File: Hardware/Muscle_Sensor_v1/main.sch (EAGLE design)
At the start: 31 parts, among them IC1 TL084D, IC2 TL7660D, K1 61000418221, K2 61000418221, U1 AD8221AR

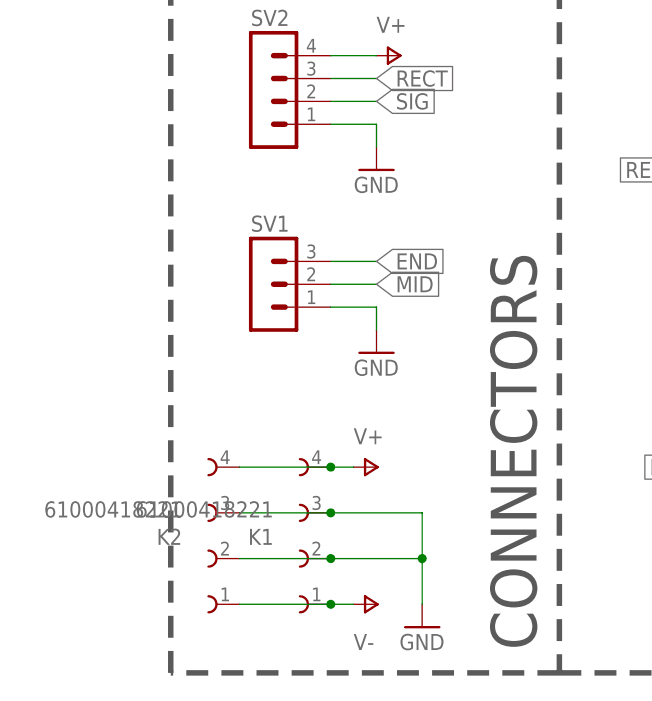
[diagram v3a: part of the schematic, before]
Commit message: Muscle Sensor Updates
Schematic and board updates fixes some bugs of first version.
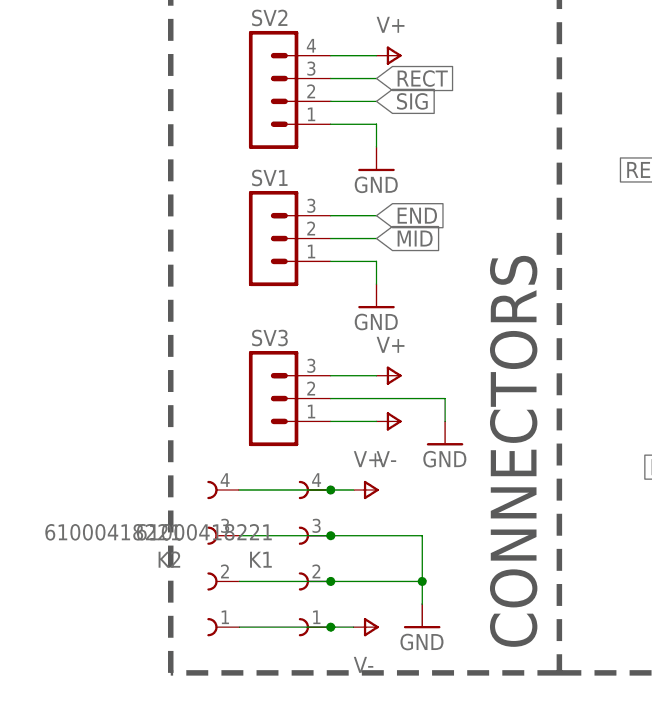
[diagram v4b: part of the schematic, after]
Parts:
- added SV3: (no value), con-lstb:MA03-1
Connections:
- net GND: now also SV3.2
- net V+: now also SV3.3
- net V-: now also SV3.1
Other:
- moved on the sheet: K1, K2, SV1
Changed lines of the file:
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@@
 <part name="H1" library="holes" library_urn="urn:adsk.eagle:library:237" deviceset="MOUNT-HOLE" device="3.0" package3d_urn="urn:adsk.eagle:package:14277/1"/>
 <part name="H2" library="holes" library_urn="urn:adsk.eagle:library:237" deviceset="MOUNT-HOLE" device="3.0" package3d_urn="urn:adsk.eagle:package:14277/1"/>
+<part name="SV3" library="con-lstb" library_urn="urn:adsk.eagle:library:162" deviceset="MA03-1" device="" package3d_urn="urn:adsk.eagle:package:8339/1"/>
+<part name="P+7" library="supply1" library_urn="urn:adsk.eagle:library:371" deviceset="V+" device=""/>
+<part name="GND11" library="supply1" library_urn="urn:adsk.eagle:library:371" deviceset="GND" device=""/>
+<part name="P-5" library="supply1" library_urn="urn:adsk.eagle:library:371" deviceset="V-" device=""/>
 </parts>
 <sheets>
@@
 </instance>
 <instance part="IC1" gate="P" x="5.08" y="114.3" smashed="yes"/>
-<instance part="SV1" gate="G$1" x="5.08" y="45.72" smashed="yes">
-<attribute name="VALUE" x="3.81" y="38.1" size="1.778" layer="96"/>
-<attribute name="NAME" x="3.81" y="51.562" size="1.778" layer="95"/>
-</instance>
-<instance part="P+1" gate="1" x="17.78" y="25.4" smashed="yes" rot="R270">
-<attribute name="VALUE" x="15.24" y="27.94" size="1.778" layer="96"/>
-</instance>
-<instance part="P-1" gate="1" x="17.78" y="10.16" smashed="yes" rot="R90">
-<attribute name="VALUE" x="15.24" y="5.08" size="1.778" layer="96"/>
+<instance part="SV1" gate="G$1" x="5.08" y="50.8" smashed="yes">
+<attribute name="VALUE" x="3.81" y="43.18" size="1.778" layer="96"/>
+<attribute name="NAME" x="3.81" y="56.642" size="1.778" layer="95"/>
+</instance>
+<instance part="P+1" gate="1" x="17.78" y="22.86" smashed="yes" rot="R270">
+<attribute name="VALUE" x="15.24" y="25.4" size="1.778" layer="96"/>
+</instance>
+<instance part="P-1" gate="1" x="17.78" y="7.62" smashed="yes" rot="R90">
+<attribute name="VALUE" x="15.24" y="2.54" size="1.778" layer="96"/>
 </instance>
 <instance part="GND1" gate="1" x="22.86" y="7.62" smashed="yes">
@@
 <attribute name="VALUE" x="15.24" y="55.88" size="1.778" layer="96"/>
 </instance>
-<instance part="GND3" gate="1" x="17.78" y="38.1" smashed="yes">
-<attribute name="VALUE" x="15.24" y="35.56" size="1.778" layer="96"/>
+<instance part="GND3" gate="1" x="17.78" y="43.18" smashed="yes">
+<attribute name="VALUE" x="15.24" y="40.64" size="1.778" layer="96"/>
 </instance>
 <instance part="P+2" gate="1" x="5.08" y="129.54" smashed="yes">
@@
 <attribute name="VALUE" x="44.323" y="157.9626" size="1.778" layer="96"/>
 </instance>
-<instance part="K1" gate="G$1" x="5.08" y="17.78" smashed="yes" rot="R180">
-<attribute name="NAME" x="6.35" y="18.542" size="1.778" layer="95" rot="R180"/>
-<attribute name="VALUE" x="6.35" y="21.59" size="1.778" layer="96" rot="R180"/>
-</instance>
-<instance part="K2" gate="G$1" x="-5.08" y="17.78" smashed="yes" rot="R180">
-<attribute name="NAME" x="-3.81" y="18.542" size="1.778" layer="95" rot="R180"/>
-<attribute name="VALUE" x="-3.81" y="21.59" size="1.778" layer="96" rot="R180"/>
+<instance part="K1" gate="G$1" x="5.08" y="15.24" smashed="yes" rot="R180">
+<attribute name="NAME" x="6.35" y="16.002" size="1.778" layer="95" rot="R180"/>
+<attribute name="VALUE" x="6.35" y="19.05" size="1.778" layer="96" rot="R180"/>
+</instance>
+<instance part="K2" gate="G$1" x="-5.08" y="15.24" smashed="yes" rot="R180">
+<attribute name="NAME" x="-3.81" y="16.002" size="1.778" layer="95" rot="R180"/>
+<attribute name="VALUE" x="-3.81" y="19.05" size="1.778" layer="96" rot="R180"/>
 </instance>
 <instance part="R10" gate="G$1" x="152.4" y="66.04" smashed="yes" rot="R90">
@@
 <attribute name="NAME" x="14.732" y="92.0242" size="1.778" layer="95"/>
 <attribute name="VALUE" x="14.732" y="88.9762" size="1.778" layer="96"/>
+</instance>
+<instance part="SV3" gate="G$1" x="5.08" y="33.02" smashed="yes">
+<attribute name="VALUE" x="3.81" y="25.4" size="1.778" layer="96"/>
+<attribute name="NAME" x="3.81" y="38.862" size="1.778" layer="95"/>
+</instance>
+<instance part="P+7" gate="1" x="20.32" y="35.56" smashed="yes" rot="R270">
+<attribute name="VALUE" x="17.78" y="38.1" size="1.778" layer="96"/>
+</instance>
+<instance part="GND11" gate="1" x="25.4" y="27.94" smashed="yes">
+<attribute name="VALUE" x="22.86" y="25.4" size="1.778" layer="96"/>
+</instance>
+<instance part="P-5" gate="1" x="20.32" y="30.48" smashed="yes" rot="R90">
+<attribute name="VALUE" x="17.78" y="25.4" size="1.778" layer="96"/>
 </instance>
 </instances>
@@
 <segment>
 <pinref part="SV1" gate="G$1" pin="1"/>
-<wire x1="17.78" y1="43.18" x2="12.7" y2="43.18" width="0.1524" layer="91"/>
-<wire x1="17.78" y1="40.64" x2="17.78" y2="43.18" width="0.1524" layer="91"/>
+<wire x1="17.78" y1="48.26" x2="12.7" y2="48.26" width="0.1524" layer="91"/>
+<wire x1="17.78" y1="45.72" x2="17.78" y2="48.26" width="0.1524" layer="91"/>
 <pinref part="GND3" gate="1" pin="GND"/>
 </segment>
 <segment>
-<wire x1="12.7" y1="15.24" x2="22.86" y2="15.24" width="0.1524" layer="91"/>
-<wire x1="22.86" y1="15.24" x2="22.86" y2="10.16" width="0.1524" layer="91"/>
+<wire x1="12.7" y1="12.7" x2="22.86" y2="12.7" width="0.1524" layer="91"/>
+<wire x1="22.86" y1="12.7" x2="22.86" y2="10.16" width="0.1524" layer="91"/>
 <pinref part="GND1" gate="1" pin="GND"/>
 <pinref part="K1" gate="G$1" pin="2"/>
 <pinref part="K1" gate="G$1" pin="3"/>
-<wire x1="12.7" y1="20.32" x2="22.86" y2="20.32" width="0.1524" layer="91"/>
-<wire x1="22.86" y1="20.32" x2="22.86" y2="15.24" width="0.1524" layer="91"/>
-<junction x="22.86" y="15.24"/>
+<wire x1="12.7" y1="17.78" x2="22.86" y2="17.78" width="0.1524" layer="91"/>
+<wire x1="22.86" y1="17.78" x2="22.86" y2="12.7" width="0.1524" layer="91"/>
+<junction x="22.86" y="12.7"/>
 <pinref part="K2" gate="G$1" pin="3"/>
-<wire x1="12.7" y1="20.32" x2="2.54" y2="20.32" width="0.1524" layer="91"/>
-<junction x="12.7" y="20.32"/>
+<wire x1="12.7" y1="17.78" x2="2.54" y2="17.78" width="0.1524" layer="91"/>
+<junction x="12.7" y="17.78"/>
 <pinref part="K2" gate="G$1" pin="2"/>
-<wire x1="12.7" y1="15.24" x2="2.54" y2="15.24" width="0.1524" layer="91"/>
-<junction x="12.7" y="15.24"/>
+<wire x1="12.7" y1="12.7" x2="2.54" y2="12.7" width="0.1524" layer="91"/>
+<junction x="12.7" y="12.7"/>
 </segment>
 <segment>
@@
 <pinref part="C2" gate="G$1" pin="-"/>
 </segment>
+<segment>
+<pinref part="GND11" gate="1" pin="GND"/>
+<wire x1="25.4" y1="30.48" x2="25.4" y2="33.02" width="0.1524" layer="91"/>
+<pinref part="SV3" gate="G$1" pin="2"/>
+<wire x1="25.4" y1="33.02" x2="12.7" y2="33.02" width="0.1524" layer="91"/>
+</segment>
 </net>
 <net name="MID" class="0">
 <segment>
 <pinref part="SV1" gate="G$1" pin="2"/>
-<wire x1="17.78" y1="45.72" x2="12.7" y2="45.72" width="0.1524" layer="91"/>
-<label x="17.78" y="45.72" size="1.778" layer="95" xref="yes"/>
+<wire x1="17.78" y1="50.8" x2="12.7" y2="50.8" width="0.1524" layer="91"/>
+<label x="17.78" y="50.8" size="1.778" layer="95" xref="yes"/>
 </segment>
 <segment>
@@
 <segment>
 <pinref part="SV1" gate="G$1" pin="3"/>
-<wire x1="17.78" y1="48.26" x2="12.7" y2="48.26" width="0.1524" layer="91"/>
-<label x="17.78" y="48.26" size="1.778" layer="95" xref="yes"/>
+<wire x1="17.78" y1="53.34" x2="12.7" y2="53.34" width="0.1524" layer="91"/>
+<label x="17.78" y="53.34" size="1.778" layer="95" xref="yes"/>
 </segment>
 <segment>
@@
 <net name="V-" class="0">
 <segment>
-<wire x1="15.24" y1="10.16" x2="12.7" y2="10.16" width="0.1524" layer="91"/>
+<wire x1="15.24" y1="7.62" x2="12.7" y2="7.62" width="0.1524" layer="91"/>
 <pinref part="P-1" gate="1" pin="V-"/>
 <pinref part="K1" gate="G$1" pin="1"/>
 <pinref part="K2" gate="G$1" pin="1"/>
-<wire x1="12.7" y1="10.16" x2="2.54" y2="10.16" width="0.1524" layer="91"/>
-<junction x="12.7" y="10.16"/>
+<wire x1="12.7" y1="7.62" x2="2.54" y2="7.62" width="0.1524" layer="91"/>
+<junction x="12.7" y="7.62"/>
 </segment>
 <segment>
@@
 <pinref part="C4" gate="G$1" pin="-"/>
 </segment>
+<segment>
+<pinref part="P-5" gate="1" pin="V-"/>
+<pinref part="SV3" gate="G$1" pin="1"/>
+<wire x1="17.78" y1="30.48" x2="12.7" y2="30.48" width="0.1524" layer="91"/>
+</segment>
 </net>
 <net name="V+" class="0">
 <segment>
-<wire x1="15.24" y1="25.4" x2="12.7" y2="25.4" width="0.1524" layer="91"/>
+<wire x1="15.24" y1="22.86" x2="12.7" y2="22.86" width="0.1524" layer="91"/>
 <pinref part="P+1" gate="1" pin="V+"/>
 <pinref part="K1" gate="G$1" pin="4"/>
 <pinref part="K2" gate="G$1" pin="4"/>
-<wire x1="12.7" y1="25.4" x2="2.54" y2="25.4" width="0.1524" layer="91"/>
-<junction x="12.7" y="25.4"/>
+<wire x1="12.7" y1="22.86" x2="2.54" y2="22.86" width="0.1524" layer="91"/>
+<junction x="12.7" y="22.86"/>
 </segment>
 <segment>
@@
 <pinref part="P+6" gate="1" pin="V+"/>
 </segment>
+<segment>
+<pinref part="P+7" gate="1" pin="V+"/>
+<pinref part="SV3" gate="G$1" pin="3"/>
+<wire x1="17.78" y1="35.56" x2="12.7" y2="35.56" width="0.1524" layer="91"/>
+</segment>
 </net>
